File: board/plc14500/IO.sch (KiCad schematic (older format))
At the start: 15 parts

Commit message: Schema
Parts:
- removed U?: 4099, symbol 4xxx_IEEE:4099
- added C1, C2, C3: 100nF, symbol Device:C
- added D1, D14, D17, D2, D3, D4, D5, D6, D7, D8: LED5MM, LED_5MM, symbol SparkFun-LED:LED5MM
- added R1, R10, R11, R12, R2, R21, R3, R4, R9: 47K, symbol Device:R
- added R13, R14, R15, R16, R17, R25, R27, R5, R6, R7, R8: 680R, symbol Device:R
- added S1, S10, S11, S12, S17, S2, S3, S4, S9: SW_Push, symbol Switch:SW_Push
- added S13, S14, S15, S16, S5, S6, S7, S8: SWITCH-DPDT-PTH-GPI-152-3013, SWITCH_DPDT_PTH_GPI-152-3013, symbol SparkFun-Switches:SWITCH-DPDT-PTH-GPI-152-3013
- added U1, U3: 74HC14, symbol 74xx:74HC14
- added U2: 4051, symbol 4xxx:4051
- added U4: Arduino Nano, Module:Arduino_Nano, symbol MCU_Module:Arduino_Nano_v2.x
- added U5: CD4099, symbol plc14500:CD4099
- gave numbers to parts that had none: 14
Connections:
- net labels added: +5V, A0, A1, A2, A3, A4, A5, A6, A7, ADDR, D, D0, D1, D2, D3, D4, D5, D6, DATA, IN0, IN1, IN2, IN3, IN4, IN5, IN6, IN7, PRG, RES, W, WEN
- wire segments 35 -> 226
- no-connect marks 0 -> 33
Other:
- note added: "Input"
- note added: "Output"
- note added: "Programming I/F"
- moved on the sheet: D10, D11, D12, D13, D15, D16, D9, R18, R19, R20, R22, R23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

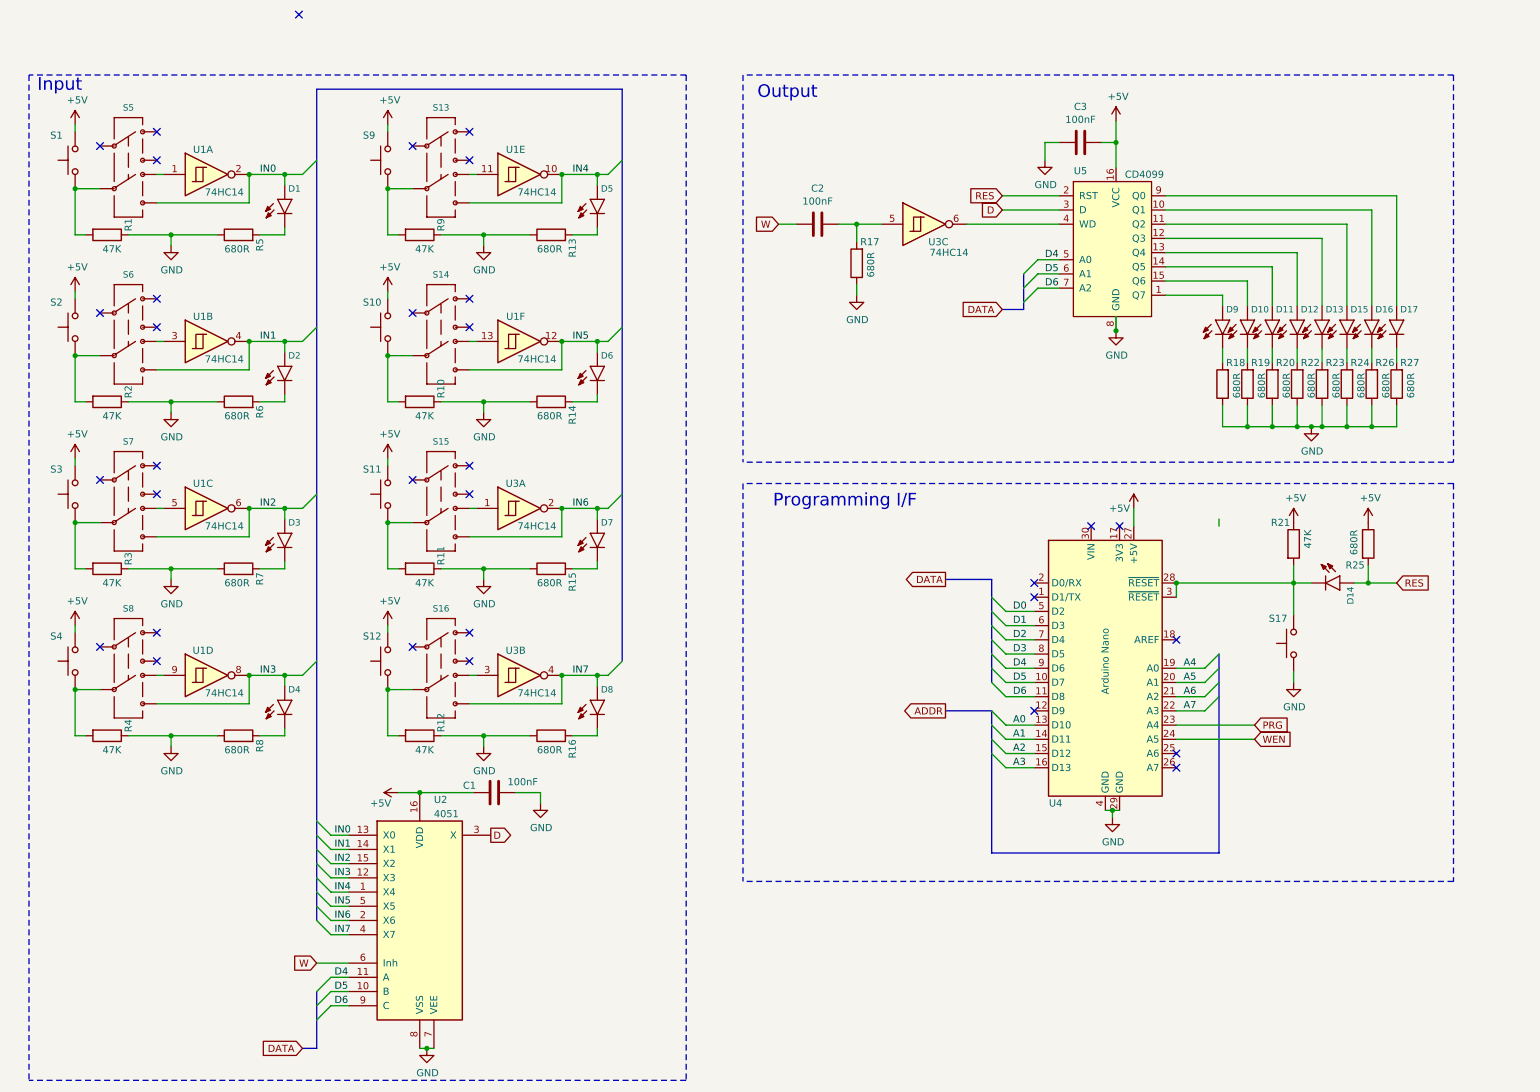
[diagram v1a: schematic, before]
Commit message: Schema updates, add loopback and timer
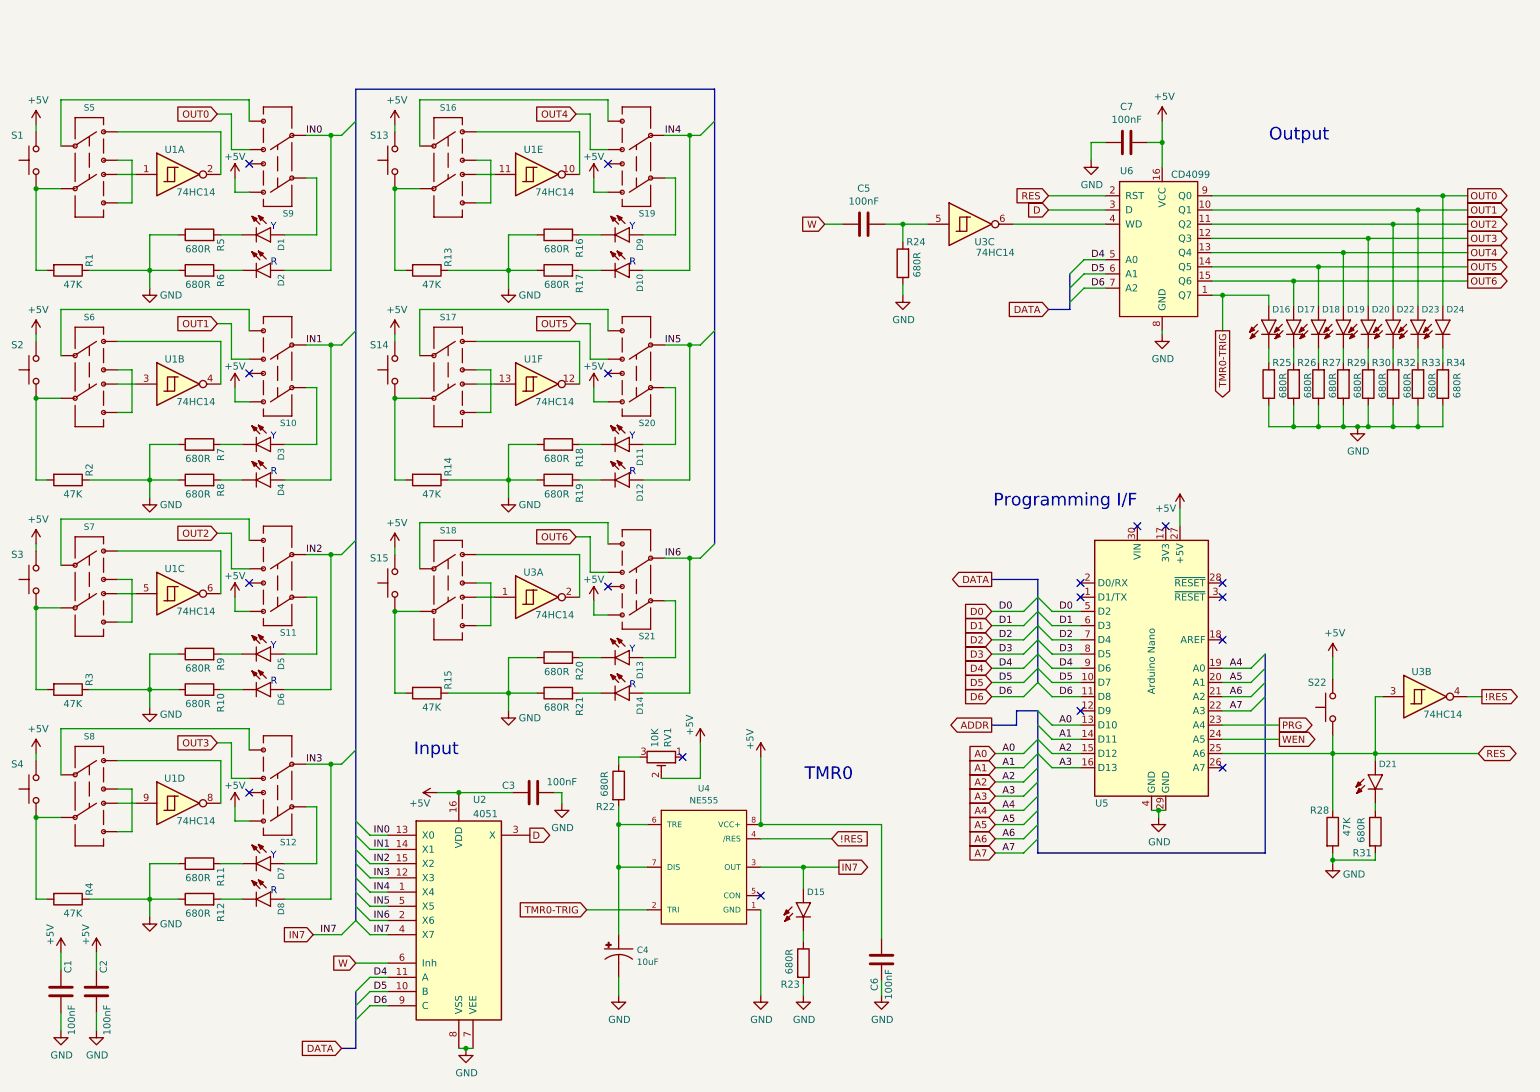
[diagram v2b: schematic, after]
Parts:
- removed D2: LED5MM, LED_5MM, symbol SparkFun-LED:LED5MM
- removed R6: 680R, symbol Device:R
- removed S10, S11, S12, S9: SW_Push, symbol Switch:SW_Push
- removed S13, S14, S15: SWITCH-DPDT-PTH-GPI-152-3013, SWITCH_DPDT_PTH_GPI-152-3013, symbol SparkFun-Switches:SWITCH-DPDT-PTH-GPI-152-3013
- added C1, C2, C6: 100nF, Capacitor_THT:C_Rect_L7.2mm_W2.5mm_P5.00mm_FKS2_FKP2_MKS2_MKP2, symbol Device:C
- added C4: 10uF, Capacitor_THT:CP_Radial_D8.0mm_P5.00mm, symbol SparkFun-Capacitors:1000UF-RADIAL-5MM-25V-20%
- added D1, D11, D13, D9: LED 5MM Yellow, plc14500:LED_5MM, symbol SparkFun-LED:LED5MM
- added D10, D12, D14: LED 5MM Red, plc14500:LED_5MM, symbol SparkFun-LED:LED5MM
- added D15: LED5MM, plc14500:LED_5MM, symbol SparkFun-LED:LED5MM
- added R17, R18, R19, R20, R21, R22, R23, R5: 680R, Resistor_THT:R_Axial_DIN0309_L9.0mm_D3.2mm_P12.70mm_Horizontal, symbol Device:R
- added RV1: 10K, Potentiometer_THT:Potentiometer_ACP_CA9-H5_Horizontal, symbol Device:R_POT_TRIM
- added S10, S11, S12, S17, S18, S19, S20, S21, S9: SWITCH-DPDT-PTH-GPI-152-3013, plc14500:SWITCH_DPDT, symbol SparkFun-Switches:SWITCH-DPDT-PTH-GPI-152-3013
- added S13, S14, S15: SW_Push, Button_Switch_THT:SW_Tactile_Straight_KSA0Axx1LFTR, symbol Switch:SW_Push
- added U4: NE555, Package_DIP:DIP-8_W7.62mm, symbol SparkFun-IC-Special-Function:555D
- C3: renamed from C1; footprint (none) -> Capacitor_THT:C_Rect_L7.2mm_W2.5mm_P5.00mm_FKS2_FKP2_MKS2_MKP2
- C5: renamed from C2; footprint (none) -> Capacitor_THT:C_Rect_L7.2mm_W2.5mm_P5.00mm_FKS2_FKP2_MKS2_MKP2
- C7: renamed from C3; footprint (none) -> Capacitor_THT:C_Rect_L7.2mm_W2.5mm_P5.00mm_FKS2_FKP2_MKS2_MKP2
- D16: renamed from D9; footprint LED_5MM -> plc14500:LED_5MM
- D17: renamed from D10; footprint LED_5MM -> plc14500:LED_5MM
- D18: renamed from D11; footprint LED_5MM -> plc14500:LED_5MM
- D19: renamed from D12; footprint LED_5MM -> plc14500:LED_5MM
- D2: renamed from D1; value LED5MM -> LED 5MM Red; footprint LED_5MM -> plc14500:LED_5MM
- D20: renamed from D13; footprint LED_5MM -> plc14500:LED_5MM
- D21: renamed from D14; footprint LED_5MM -> plc14500:LED_5MM
- D22: renamed from D15; footprint LED_5MM -> plc14500:LED_5MM
- D23: renamed from D16; footprint LED_5MM -> plc14500:LED_5MM
- D24: renamed from D17; footprint LED_5MM -> plc14500:LED_5MM
- D3, D5, D7: value LED5MM -> LED 5MM Yellow; footprint LED_5MM -> plc14500:LED_5MM
- D4, D6, D8: value LED5MM -> LED 5MM Red; footprint LED_5MM -> plc14500:LED_5MM
- R1, R16, R2, R3, R4, R7, R8: footprint (none) -> Resistor_THT:R_Axial_DIN0309_L9.0mm_D3.2mm_P12.70mm_Horizontal
- R10, R11, R12, R9: value 47K -> 680R; footprint (none) -> Resistor_THT:R_Axial_DIN0309_L9.0mm_D3.2mm_P12.70mm_Horizontal
- R13, R14, R15: value 680R -> 47K; footprint (none) -> Resistor_THT:R_Axial_DIN0309_L9.0mm_D3.2mm_P12.70mm_Horizontal
- R24: renamed from R17; footprint (none) -> Resistor_THT:R_Axial_DIN0309_L9.0mm_D3.2mm_P12.70mm_Horizontal
- R25: renamed from R18; footprint (none) -> Resistor_THT:R_Axial_DIN0309_L9.0mm_D3.2mm_P12.70mm_Horizontal
- R26: renamed from R19; footprint (none) -> Resistor_THT:R_Axial_DIN0309_L9.0mm_D3.2mm_P12.70mm_Horizontal
- R27: renamed from R20; footprint (none) -> Resistor_THT:R_Axial_DIN0309_L9.0mm_D3.2mm_P12.70mm_Horizontal
- R28: renamed from R21; footprint (none) -> Resistor_THT:R_Axial_DIN0309_L9.0mm_D3.2mm_P12.70mm_Horizontal
- R29: renamed from R22; footprint (none) -> Resistor_THT:R_Axial_DIN0309_L9.0mm_D3.2mm_P12.70mm_Horizontal
- R30: renamed from R23; footprint (none) -> Resistor_THT:R_Axial_DIN0309_L9.0mm_D3.2mm_P12.70mm_Horizontal
- R31: renamed from R25; footprint (none) -> Resistor_THT:R_Axial_DIN0309_L9.0mm_D3.2mm_P12.70mm_Horizontal
- R32: renamed from R24; footprint (none) -> Resistor_THT:R_Axial_DIN0309_L9.0mm_D3.2mm_P12.70mm_Horizontal
- R33: renamed from R26; footprint (none) -> Resistor_THT:R_Axial_DIN0309_L9.0mm_D3.2mm_P12.70mm_Horizontal
- R34: renamed from R27; footprint (none) -> Resistor_THT:R_Axial_DIN0309_L9.0mm_D3.2mm_P12.70mm_Horizontal
- R6: renamed from R5; footprint (none) -> Resistor_THT:R_Axial_DIN0309_L9.0mm_D3.2mm_P12.70mm_Horizontal
- S1, S2, S3, S4: footprint (none) -> Button_Switch_THT:SW_Tactile_Straight_KSA0Axx1LFTR
- S16, S5, S6, S7, S8: footprint SWITCH_DPDT_PTH_GPI-152-3013 -> plc14500:SWITCH_DPDT
- S22: renamed from S17; footprint (none) -> Button_Switch_THT:SW_Tactile_Straight_KSA0Axx1LFTR
- U1, U3: footprint (none) -> Package_DIP:DIP-14_W7.62mm_LongPads
- U2: footprint (none) -> Package_DIP:DIP-16_W7.62mm_LongPads; Order (none) -> https://www.aliexpress.com/item/1005003598992135.html?spm=a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; Price (none) -> 0.85
- U6: renamed from U5; footprint (none) -> Package_DIP:DIP-16_W7.62mm_LongPads
- renumbered U4 to U5
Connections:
- net +5V: now also S22.2, C1.2, C2.2, C6.1, RV1.2, S10.1, S11.1, S12.1, S13.2, S14.2, S15.2, S19.1, S20.1, S21.1, S9.1, U4.8 (VCC+); no longer R28.1, R31.1
- net GND: now also R28.2, R31.2, C1.1, C2.1, C4.-, C6.2, R17.1, R18.1, R19.1, R20.1, R21.1, R23.2, R5.1, U4.1 (GND); no longer S22.1
- net IN0: now also S9.6; no longer S5.7, U1.2
- net IN1: now also D4.A, S10.6; no longer S6.7, U1.4
- net IN2: now also D6.A, S11.6; no longer D3.A, S7.7, U1.6
- net IN3: now also D8.A, S12.6; no longer D4.A, S8.7, U1.8
- net IN4: now also D10.A, S19.6; no longer D5.A, U1.10
- net IN5: now also D12.A, S20.6; no longer D6.A, U1.12
- net IN6: now also D14.A, S21.6; no longer D7.A, U3.2
- net IN7: now also D15.A, U4.3 (OUT); no longer D8.A, S16.7, U3.4
- net RES: now also R28.1, S22.1, U3.3, U5.25 (A6); no longer R31.2
- net TMR0-TRIG: now reaches D16.A, U6.1 (Q7)
- net TMR0-TRIG: now also U4.2 (TRI)
- net OUT1: now reaches D23.A, U6.10 (Q1)
- net OUT1: now also S10.5
- net OUT2: now reaches D22.A, U6.11 (Q2)
- net OUT2: now also S11.5
- net OUT3: now reaches D20.A, U6.12 (Q3)
- net OUT3: now also S12.5
- net OUT4: now reaches D19.A, U6.13 (Q4)
- net OUT4: now also S19.5
- net OUT5: now reaches D18.A, U6.14 (Q5)
- net OUT5: now also S20.5
- net OUT6: now reaches D17.A, U6.15 (Q6)
- net OUT6: now also S21.5
- net OUT0: now reaches D24.A, U6.9 (Q0)
- net OUT0: now also S9.5
- net at S5.1: now also U1.2
- net at S5.2: now also S9.7
- net at S5.3: now also S5.7
- net at S6.1: now also U1.4
- net at S6.2: now also S10.7
- net at S6.3: now also S6.7
- net at S7.1: now also U1.6
- net at S7.2: now also S11.7
- net at S7.3: now also S7.7
- net at S8.1: now also U1.8
- net at S8.2: now also S12.7
- net at S8.3: now also S8.7
- net at U1.11: now also S16.5
- net at R9.2: now also D5.K (C)
- net at R13.2: now also S16.6, S13.1; no longer D5.K (C)
- net at U1.13: now also S17.5
- net at R10.2: now also D6.K (C)
- net at R14.2: now also S14.1, S17.6; no longer D6.K (C)
- net at U3.1: now also S18.5
- net at R11.2: now also D7.K (C)
- net at R15.2: now also S15.1, S18.6; no longer D7.K (C)
- net at S16.1: now also U1.10
- net at S16.2: now also S19.7
- net at S16.3: now also S16.7
- net at R12.2: now also D8.K (C); no longer S16.6
- net at R16.2: now also D9.K (C); no longer D8.K (C)
- new net: D21.K (C), R31.1
- new net: C4.+, R22.2, U4.6 (TRE), U4.7 (DIS)
- new net: R22.1, RV1.3
- new net: D15.K (C), R23.1
- new net: D1.A, S9.2
- new net: D1.K (C), R5.2
- new net: D3.A, S10.2
- new net: D5.A, S11.2
- new net: D7.A, S12.2
- new net: D10.K (C), R17.2
- new net: D9.A, S19.2
- new net: S17.1, U1.12
- new net: S17.2, S20.7
- new net: S17.3, S17.7
- new net: D12.K (C), R19.2
- new net: D11.A, S20.2
- new net: D11.K (C), R18.2
- new net: S18.1, U3.2
- new net: S18.2, S21.7
- new net: S18.3, S18.7
- new net: D14.K (C), R21.2
- new net: D13.A, S21.2
- new net: D13.K (C), R20.2
- new net !RES: U3.4, U4.4 (/RES)
- now unconnected: U5.28 (~RESET), U5.3 (~RESET)
- no-connect marks 33 -> 18
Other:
- note added: "R"
- note added: "TMR0"
- note added: "Y"
- moved on the sheet: C3, C5, C7, D16, D17, D18, D19, D2, D20, D21, D22, D23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

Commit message: Add assembler skeleton
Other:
- moved on the sheet: C5, C7, D16, D17, D18, D19, D20, D22, D23, D24, R24, R25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

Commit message: Add scratchpad ram
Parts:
- removed C5: 100nF, Capacitor_THT:C_Rect_L7.2mm_W2.5mm_P5.00mm_FKS2_FKP2_MKS2_MKP2, symbol Device:C
- removed R24: 680R, Resistor_THT:R_Axial_DIN0309_L9.0mm_D3.2mm_P12.70mm_Horizontal, symbol Device:R
- removed unit 3 of U3
- renumbered R29 to R28, R28 to R29, U5 to U8, U6 to U9
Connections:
- net D7: now reaches U8.12 (D9)
- net TMR0-TRIG renamed TMR0-TRG
- net W renamed IN-WINH
- no-connect marks 18 -> 17
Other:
- moved on the sheet: C4, C6, C7, D15, D16, D17, D18, D19, D20, D21, D22, D23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

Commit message: Schematic tweaks
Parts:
- removed D1, D11, D13, D9: LED 5MM Yellow, plc14500:LED_5MM, symbol SparkFun-LED:LED5MM
- removed D10, D12, D14, D8: LED 5MM Red, plc14500:LED_5MM, symbol SparkFun-LED:LED5MM
- removed R15: 47K, Resistor_THT:R_Axial_DIN0309_L9.0mm_D3.2mm_P12.70mm_Horizontal, symbol Device:R
- removed R16, R17, R18, R19, R20, R21, R5: 680R, Resistor_THT:R_Axial_DIN0309_L9.0mm_D3.2mm_P12.70mm_Horizontal, symbol Device:R
- removed S10, S11, S16, S17, S18, S19, S20, S21, S9: SWITCH-DPDT-PTH-GPI-152-3013, plc14500:SWITCH_DPDT, symbol SparkFun-Switches:SWITCH-DPDT-PTH-GPI-152-3013
- removed S13, S14, S15: SW_Push, Button_Switch_THT:SW_Tactile_Straight_KSA0Axx1LFTR, symbol Switch:SW_Push
- added D2: LED 5MM Red, plc14500:LED_5MM, symbol SparkFun-LED:LED5MM
- added R22: 0R, Resistor_THT:R_Axial_DIN0309_L9.0mm_D3.2mm_P12.70mm_Horizontal, symbol Device:R
- added R6: 680R, Resistor_THT:R_Axial_DIN0309_L9.0mm_D3.2mm_P12.70mm_Horizontal, symbol Device:R
- added S10, S11, S9: Push Button, Button_Switch_THT:SW_Tactile_Straight_KSA0Axx1LFTR, symbol Switch:SW_Push
- added S13, S14: Switch DPDT, plc14500:SWITCH_DPDT, symbol SparkFun-Switches:SWITCH-DPDT-PTH-GPI-152-3013
- C1, C2, C3: Price (none) -> 0.02
- C4: Price (none) -> 0.04
- C5: renamed from C6; Price (none) -> 0.02
- C6: renamed from C7; Price (none) -> 0.02
- D1: renamed from D2; Price (none) -> 0.01
- D10: renamed from D17; value LED5MM -> LED 5MM Red; Price (none) -> 0.01
- D11: renamed from D18; value LED5MM -> LED 5MM Red; Price (none) -> 0.01
- D12: renamed from D19; value LED5MM -> LED 5MM Red; Price (none) -> 0.01
- D13: renamed from D20; value LED5MM -> LED 5MM Red; Price (none) -> 0.01
- D14: renamed from D22; value LED5MM -> LED 5MM Red; Price (none) -> 0.01
- D15: renamed from D23; value LED5MM -> LED 5MM Red; Price (none) -> 0.01
- D16: renamed from D24; value LED5MM -> LED 5MM Red; Price (none) -> 0.01
- D17: renamed from D21; value LED5MM -> LED 5MM Red; Price (none) -> 0.01
- D3, D5, D7: value LED 5MM Yellow -> LED 5MM Red; Price (none) -> 0.01
- D4, D6, R1, R12, R2, R3, R4, R7, R8, RV1: Price (none) -> 0.01
- D8: renamed from D15; value LED5MM -> LED 5MM Red; Price (none) -> 0.01
- D9: renamed from D16; value LED5MM -> LED 5MM Red; Price (none) -> 0.01
- R10, R11, R9: value 680R -> 47K; Price (none) -> 0.01
- R13, R14: value 47K -> 680R; Price (none) -> 0.01
- R15: renamed from R22; Price (none) -> 0.01
- R16: renamed from R23; Price (none) -> 0.01
- R17: renamed from R25; Price (none) -> 0.01
- R18: renamed from R26; Price (none) -> 0.01
- R19: renamed from R27; Price (none) -> 0.01
- R20: renamed from R28; Price (none) -> 0.01
- R21: renamed from R30; Price (none) -> 0.01
- R23: renamed from R32; Price (none) -> 0.01
- R24: renamed from R33; Price (none) -> 0.01
- R25: renamed from R34; Price (none) -> 0.01
- R26: renamed from R29; Price (none) -> 0.01
- R27: renamed from R31; Price (none) -> 0.01
- R5: renamed from R6; Price (none) -> 0.01
- S1, S2, S3, S4: value SW_Push -> Push Button; Price (none) -> 0.01
- S12, S5, S6, S7, S8: value SWITCH-DPDT-PTH-GPI-152-3013 -> Switch DPDT; Price (none) -> 0.69
- S15: renamed from S22; value SW_Push -> Push Button; Price (none) -> 0.01
- U1, U3: Price (none) -> 0.16
- U4: Price (none) -> 0.07
- U5: renamed from U9; value CD4099 -> 4099; Price (none) -> 0.57
- renumbered U8 to U6
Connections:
- net +5V: now also R22.1, S10.2, S11.2, S9.2; no longer S12.1, U6.27 (+5V)
- net GND: now also R6.1
- net IN0: now also S5.2
- net IN1: now also S6.2, D2.A; no longer D4.A
- net IN2: now also D3.A, S7.2; no longer D6.A
- net IN3: now also D4.A, S8.2; no longer S12.6
- net IN4: now also D5.A, S12.2
- net IN5: now also D6.A, S13.2
- net IN6: now also D7.A, S14.2
- net OUT-WD: now reaches U5.4 (WD)
- net at R10.2: now also S10.1, S13.6; no longer D6.K (C)
- net at R9.2: now also S12.6, S9.1; no longer D5.K (C)
- net at S12.7: now also S12.3; no longer S8.2
- net at R12.2: now also D5.K (C)
- net at R11.2: now also S11.1, S14.6; no longer D7.K (C)
- net at U1.10: now also S12.1
- net at U1.11: now also S12.5
- net at R13.2: now also D6.K (C)
- net at U1.12: now also S13.1
- net at U1.13: now also S13.5
- net at R14.2: now also D7.K (C)
- net at U3.2: now also S14.1
- net at U3.1: now also S14.5
- net OUT0: no longer names the net of D16.A, U5.9 (Q0)
- net OUT1: no longer names the net of D15.A, U5.10 (Q1)
- net OUT2: no longer names the net of D14.A, U5.11 (Q2)
- net OUT3: no longer names the net of D13.A, U5.12 (Q3)
- net OUT3: no longer S12.5
- net OUT4: no longer names the net of D12.A, U5.13 (Q4)
- net OUT5: no longer names the net of D11.A, U5.14 (Q5)
- net OUT6: no longer names the net of D10.A, U5.15 (Q6)
- new net: R22.2, U6.27 (+5V)
- new net: D2.K (C), R6.2
- new net: S13.3, S13.7
- new net: S14.3, S14.7
- no-connect marks 17 -> 10
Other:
- note added: "U1, U3 power decoupling"
- note removed: "R"
- note removed: "Y"
- moved on the sheet: D1, R1, R5, S1, S5, U1A

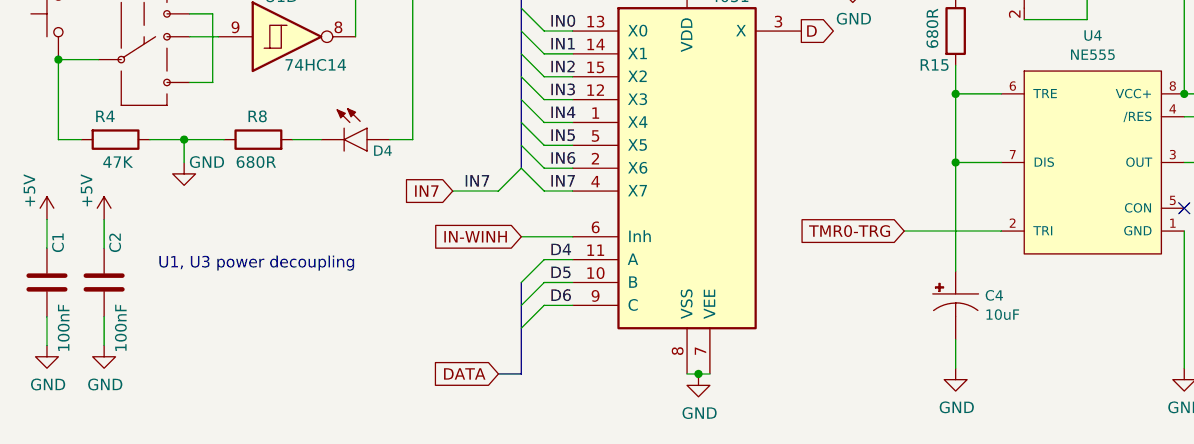
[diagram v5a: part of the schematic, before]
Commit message: All components on the board! WIP
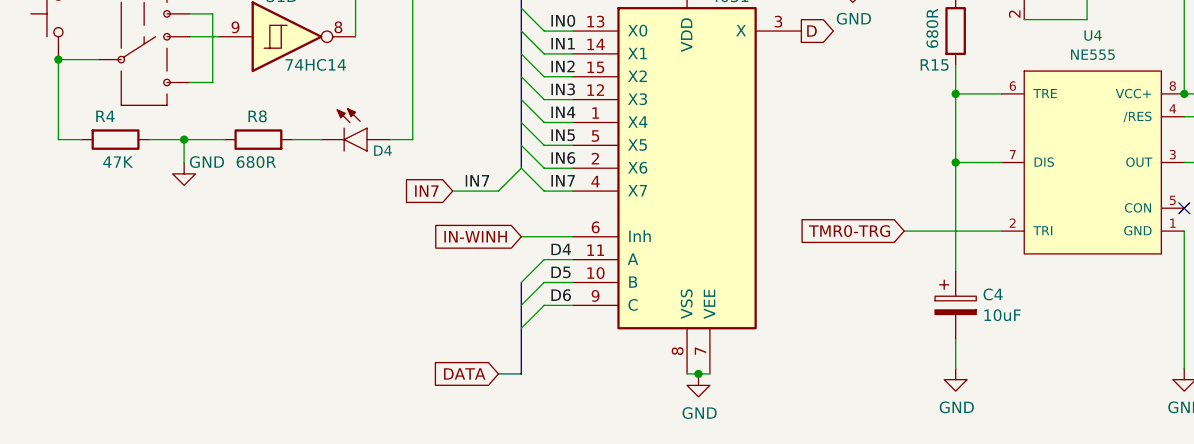
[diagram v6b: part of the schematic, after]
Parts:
- removed C1, C2: 100nF, Capacitor_THT:C_Rect_L7.2mm_W2.5mm_P5.00mm_FKS2_FKP2_MKS2_MKP2, symbol Device:C
- removed C4: 10uF, Capacitor_THT:CP_Radial_D8.0mm_P5.00mm, symbol SparkFun-Capacitors:1000UF-RADIAL-5MM-25V-20%
- added C4: 10uF, Capacitor_THT:CP_Radial_D8.0mm_P5.00mm, symbol Device:CP
- D1, D10, D11, D12, D13, D14, D15, D16, D17, D2, D3, D4, D5, D6, D7, D8, D9: footprint plc14500:LED_5MM -> plc14500:LED_3MM
- R1, R10, R11, R12, R13, R14, R15, R16, R17, R18, R19, R2, R20, R21, R22, R23, R24, R25, R26, R27, R3, R4, R5, R6, R7, R8, R9: footprint Resistor_THT:R_Axial_DIN0309_L9.0mm_D3.2mm_P12.70mm_Horizontal -> Resistor_THT:R_Axial_DIN0204_L3.6mm_D1.6mm_P7.62mm_Horizontal
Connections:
- net GND: now also C4.2
- net at R15.2, U4.6 (TRE), U4.7 (DIS): now also C4.1
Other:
- note removed: "U1, U3 power decoupling"
